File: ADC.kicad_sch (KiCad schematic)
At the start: 18 parts

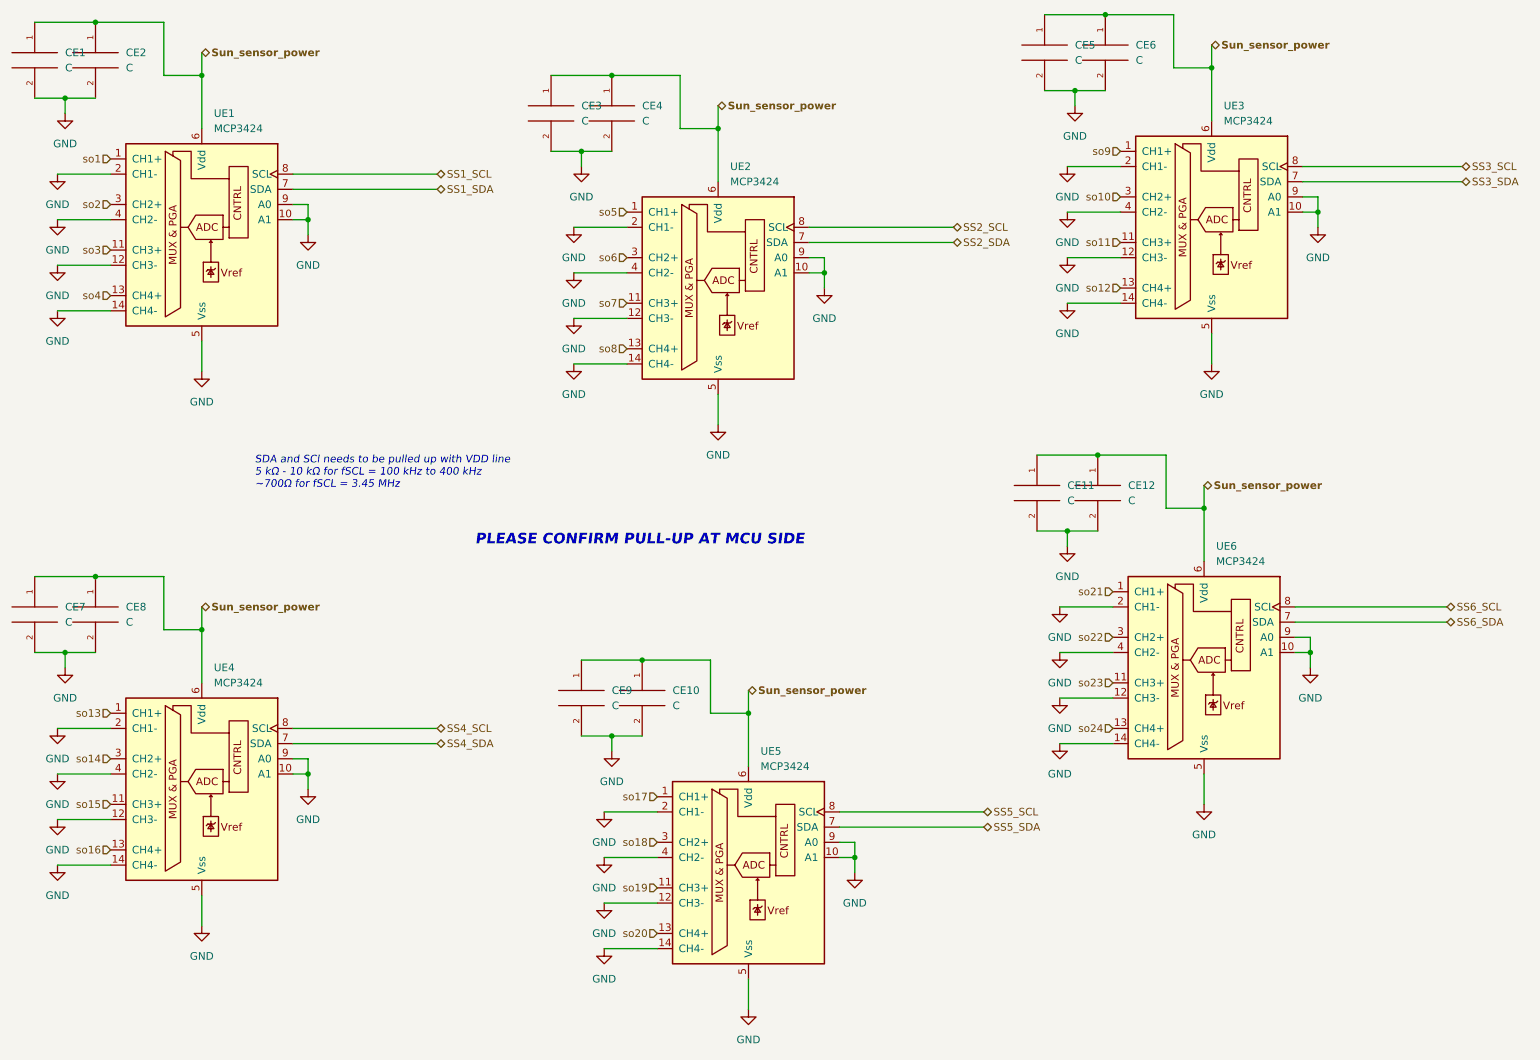
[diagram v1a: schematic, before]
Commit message: ADC Decaps added
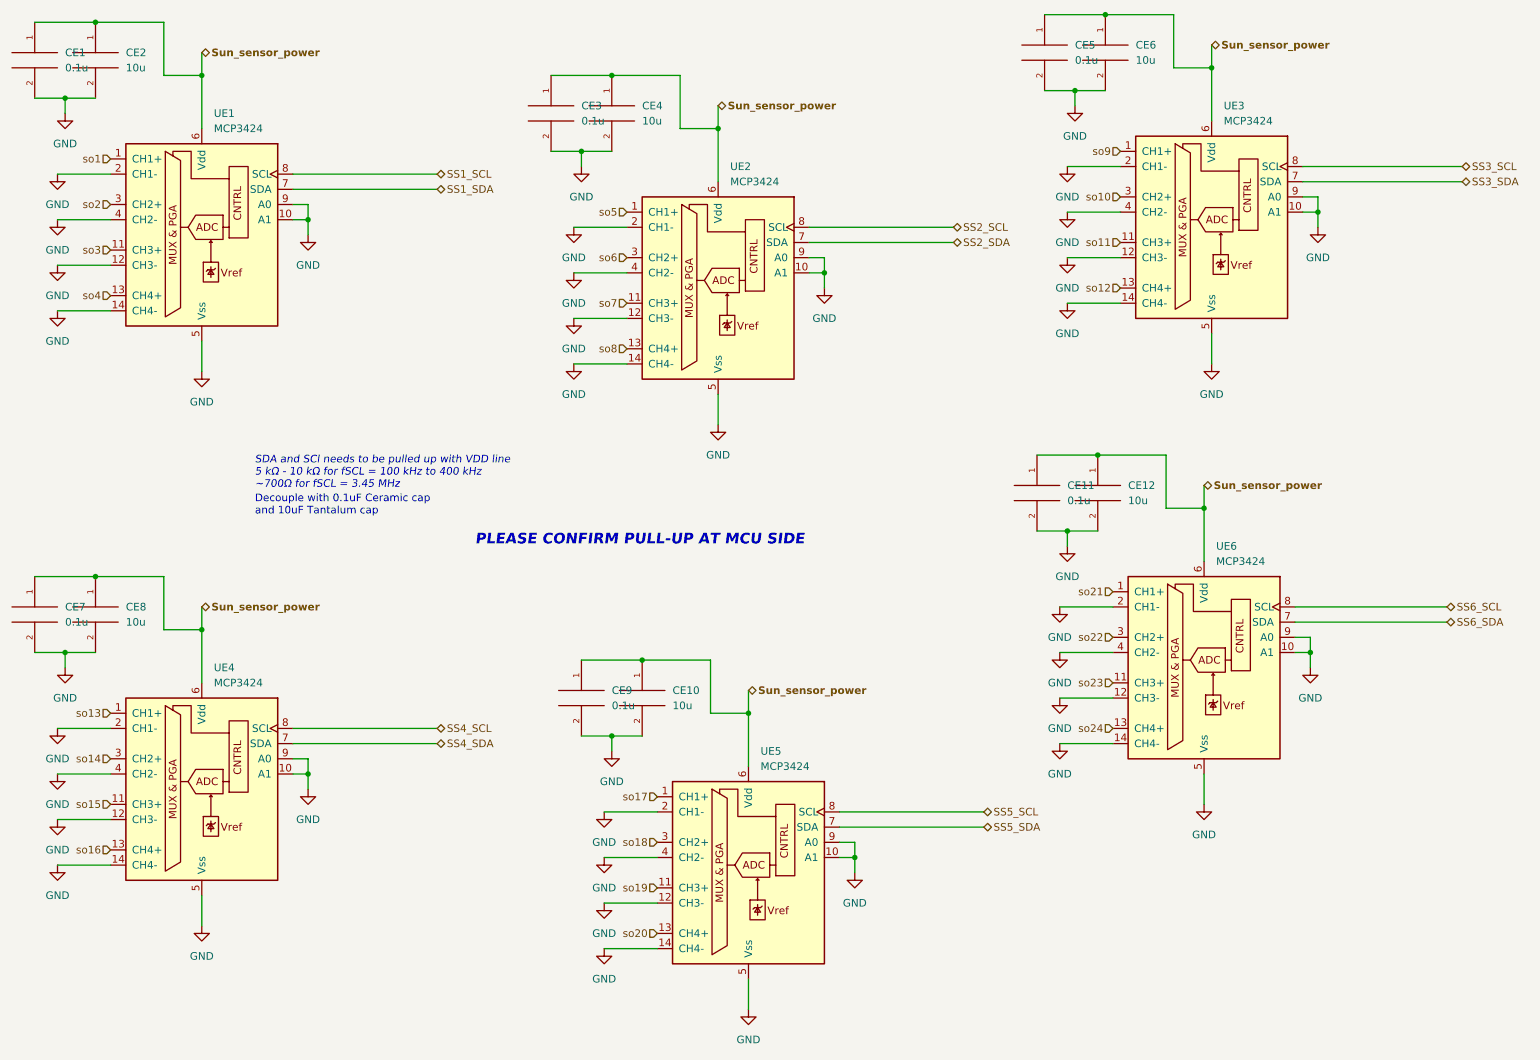
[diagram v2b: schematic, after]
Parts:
- CE1, CE11, CE3, CE5, CE7, CE9: value C -> 0.1u
- CE10, CE12, CE2, CE4, CE6, CE8: value C -> 10u
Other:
- note added: "Decouple with 0.1uF Ceramic cap and 10uF Tantalum cap"
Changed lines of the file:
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@@
     (effects (font (size 1.778 1.778) (thickness 0.3556) bold italic) (justify left bottom))
+  )
+  (text "Decouple with 0.1uF Ceramic cap \nand 10uF Tantalum cap \n"
+    (at 59.69 107.95 0)
+    (effects (font (size 1.27 1.27)) (justify left bottom))
   )
   (text "SDA and SCl needs to be pulled up with VDD line\n5 kΩ - 10 kΩ for fSCL = 100 kHz to 400 kHz\n~700Ω for fSCL = 3.45 MHz\n"
@@
       (effects (font (size 1.27 1.27)) (justify left))
     )
-    (property "Value" "C" (id 1) (at 129.54 139.6999 0)
+    (property "Value" "10u" (id 1) (at 129.54 139.6999 0)
       (effects (font (size 1.27 1.27)) (justify left))
     )
@@
       (effects (font (size 1.27 1.27)) (justify left))
     )
-    (property "Value" "C" (id 1) (at 114.3 41.9099 0)
+    (property "Value" "0.1u" (id 1) (at 114.3 41.9099 0)
       (effects (font (size 1.27 1.27)) (justify left))
     )
@@
       (effects (font (size 1.27 1.27)) (justify left))
     )
-    (property "Value" "C" (id 1) (at 119.38 139.6999 0)
+    (property "Value" "0.1u" (id 1) (at 119.38 139.6999 0)
       (effects (font (size 1.27 1.27)) (justify left))
     )
@@
       (effects (font (size 1.27 1.27)) (justify left))
     )
-    (property "Value" "C" (id 1) (at 38.1 33.0199 0)
+    (property "Value" "10u" (id 1) (at 38.1 33.0199 0)
       (effects (font (size 1.27 1.27)) (justify left))
     )
@@
       (effects (font (size 1.27 1.27)) (justify left))
     )
-    (property "Value" "C" (id 1) (at 196.85 31.7499 0)
+    (property "Value" "0.1u" (id 1) (at 196.85 31.7499 0)
       (effects (font (size 1.27 1.27)) (justify left))
     )
@@
       (effects (font (size 1.27 1.27)) (justify left))
     )
-    (property "Value" "C" (id 1) (at 195.58 105.4099 0)
+    (property "Value" "0.1u" (id 1) (at 195.58 105.4099 0)
       (effects (font (size 1.27 1.27)) (justify left))
     )
@@
       (effects (font (size 1.27 1.27)) (justify left))
     )
-    (property "Value" "C" (id 1) (at 27.94 125.7299 0)
+    (property "Value" "0.1u" (id 1) (at 27.94 125.7299 0)
       (effects (font (size 1.27 1.27)) (justify left))
     )
@@
       (effects (font (size 1.27 1.27)) (justify left))
     )
-    (property "Value" "C" (id 1) (at 207.01 31.7499 0)
+    (property "Value" "10u" (id 1) (at 207.01 31.7499 0)
       (effects (font (size 1.27 1.27)) (justify left))
     )
@@
       (effects (font (size 1.27 1.27)) (justify left))
     )
-    (property "Value" "C" (id 1) (at 38.1 125.7299 0)
+    (property "Value" "10u" (id 1) (at 38.1 125.7299 0)
       (effects (font (size 1.27 1.27)) (justify left))
     )
@@
       (effects (font (size 1.27 1.27)) (justify left))
     )
-    (property "Value" "C" (id 1) (at 124.46 41.9099 0)
+    (property "Value" "10u" (id 1) (at 124.46 41.9099 0)
       (effects (font (size 1.27 1.27)) (justify left))
     )
@@
       (effects (font (size 1.27 1.27)) (justify left))
     )
-    (property "Value" "C" (id 1) (at 205.74 105.4099 0)
+    (property "Value" "10u" (id 1) (at 205.74 105.4099 0)
       (effects (font (size 1.27 1.27)) (justify left))
     )
@@
       (effects (font (size 1.27 1.27)) (justify left))
     )
-    (property "Value" "C" (id 1) (at 27.94 33.0199 0)
-      (effects (font (size 1.27 1.27)) (justify left))
-    )
+    (property "Value" "0.1u" (id 1) (at 27.94 33.0199 0)
+      (effects (font (size 1.27 1.27)) (justify left))
+    )

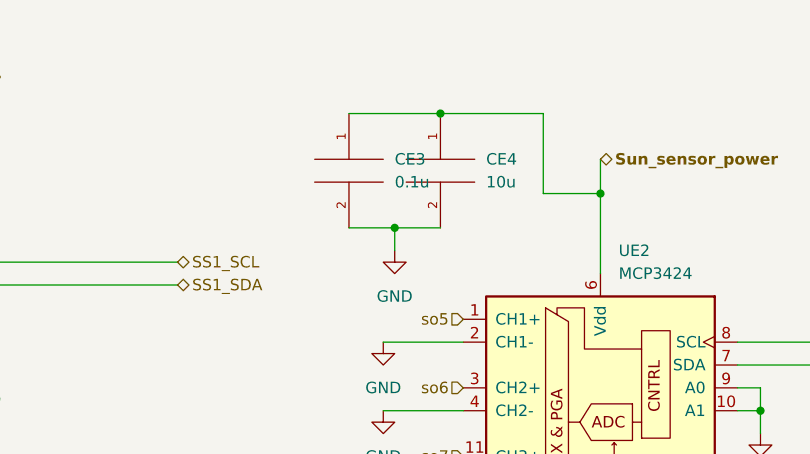
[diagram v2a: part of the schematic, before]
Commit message: Reset switch added
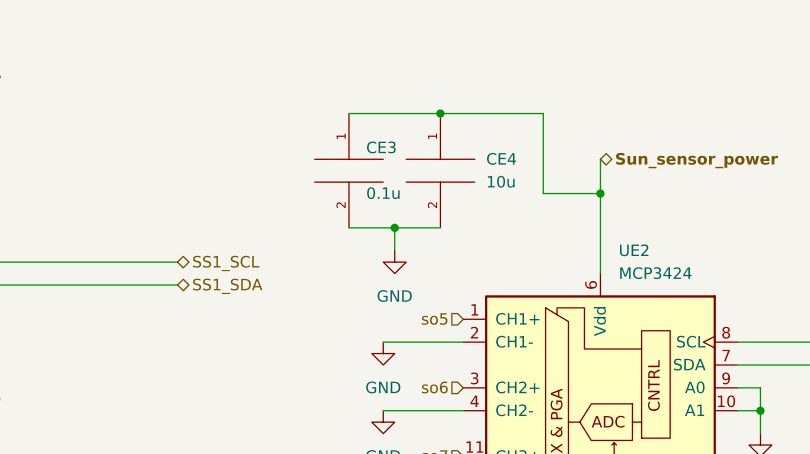
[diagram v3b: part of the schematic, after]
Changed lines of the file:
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@@
   )
   (symbol (lib_id "pspice:C") (at 109.22 40.64 0) (unit 1)
-    (in_bom yes) (on_board yes) (fields_autoplaced)
-    (property "Reference" "CE3" (id 0) (at 114.3 39.3699 0)
+    (in_bom yes) (on_board yes)
+    (property "Reference" "CE3" (id 0) (at 111.125 38.1 0)
       (effects (font (size 1.27 1.27)) (justify left))
     )
-    (property "Value" "0.1u" (id 1) (at 114.3 41.9099 0)
+    (property "Value" "0.1u" (id 1) (at 111.125 43.18 0)
       (effects (font (size 1.27 1.27)) (justify left))
     )

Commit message: MCU interfaces are done! Check the Changes and Complete ERC modifications
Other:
- company: (none) -> Parikshit Student Satellite Team
- title: (none) -> AOCS BOARD
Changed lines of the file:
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@@
 (kicad_sch (version 20211123) (generator eeschema)
   (paper "A4")
+  (title_block
+    (title "AOCS BOARD")
+    (company "Parikshit Student Satellite Team")
+  )
   (junction (at 201.93 24.13) (diameter 0) (color 0 0 0 0)
   )
@@
   )
   (wire (pts (xy 137.16 43.18) (xy 130.81 43.18))
+    (stroke (width 0) (type default) (color 0 0 0 0))
+  )
+  (wire (pts (xy 73.025 191.135) (xy 73.025 189.865))
     (stroke (width 0) (type default) (color 0 0 0 0))
   )
@@
     (pin "1")
   )
+  (symbol (lib_id "power:PWR_FLAG") (at 73.025 189.865 0) (unit 1)
+    (in_bom yes) (on_board yes) (fields_autoplaced)
+    (property "Reference" "#FLG0112" (id 0) (at 73.025 187.96 0)
+      (effects (font (size 1.27 1.27)) hide)
+    )
+    (property "Value" "PWR_FLAG" (id 1) (at 73.025 184.15 0))
+    (property "Footprint" "" (id 2) (at 73.025 189.865 0)
+      (effects (font (size 1.27 1.27)) hide)
+    )
+    (property "Datasheet" "~" (id 3) (at 73.025 189.865 0)
+      (effects (font (size 1.27 1.27)) hide)
+    )
+    (pin "1")
+  )
   (symbol (lib_id "power:GND") (at 119.38 147.32 0) (unit 1)
     (in_bom yes) (on_board yes) (fields_autoplaced)
@@
       (effects (font (size 1.27 1.27)) hide)
     )
+    (pin "1")
+  )
+  (symbol (lib_id "power:GND") (at 73.025 191.135 0) (unit 1)
+    (in_bom yes) (on_board yes) (fields_autoplaced)
+    (property "Reference" "#PWR0276" (id 0) (at 73.025 197.485 0)
+      (effects (font (size 1.27 1.27)) hide)
+    )
+    (property "Value" "GND" (id 1) (at 73.025 195.58 0))
+    (property "Footprint" "" (id 2) (at 73.025 191.135 0)
+      (effects (font (size 1.27 1.27)) hide)
+    )
+    (property "Datasheet" "" (id 3) (at 73.025 191.135 0)
+      (effects (font (size 1.27 1.27)) hide)
+    )

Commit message: Updated the changes
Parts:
- renumbered CE5 to CE1, CE8 to CE10, CE9 to CE11, CE10 to CE12, CE6 to CE2, CE1 to CE3, CE2 to CE4, CE3 to CE5, CE4 to CE6, CE11 to CE7, CE12 to CE8, CE7 to CE9, UE3 to UE1, UE1 to UE2, UE2 to UE3, UE6 to UE4, UE4 to UE5, UE5 to UE6

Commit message: Page settings changed. Added some testpoints. Some comments are made.
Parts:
- renumbered CE3 to CE1, CE1 to CE10, CE8 to CE11, CE2 to CE12, CE9 to CE2, CE4 to CE3, CE10 to CE4, CE11 to CE6, CE6 to CE7, CE12 to CE8, CE7 to CE9, UE2 to UE1, UE5 to UE2, UE6 to UE4, UE4 to UE5, UE1 to UE6

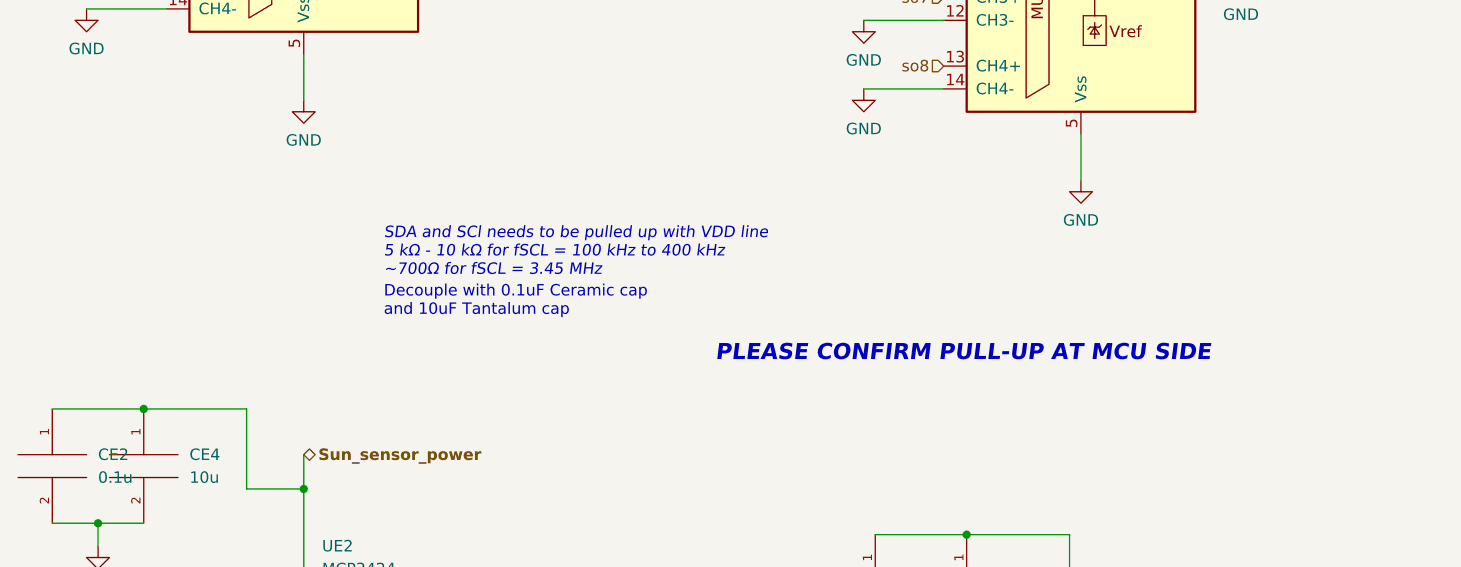
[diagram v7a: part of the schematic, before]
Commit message: I2C lines are pulled up
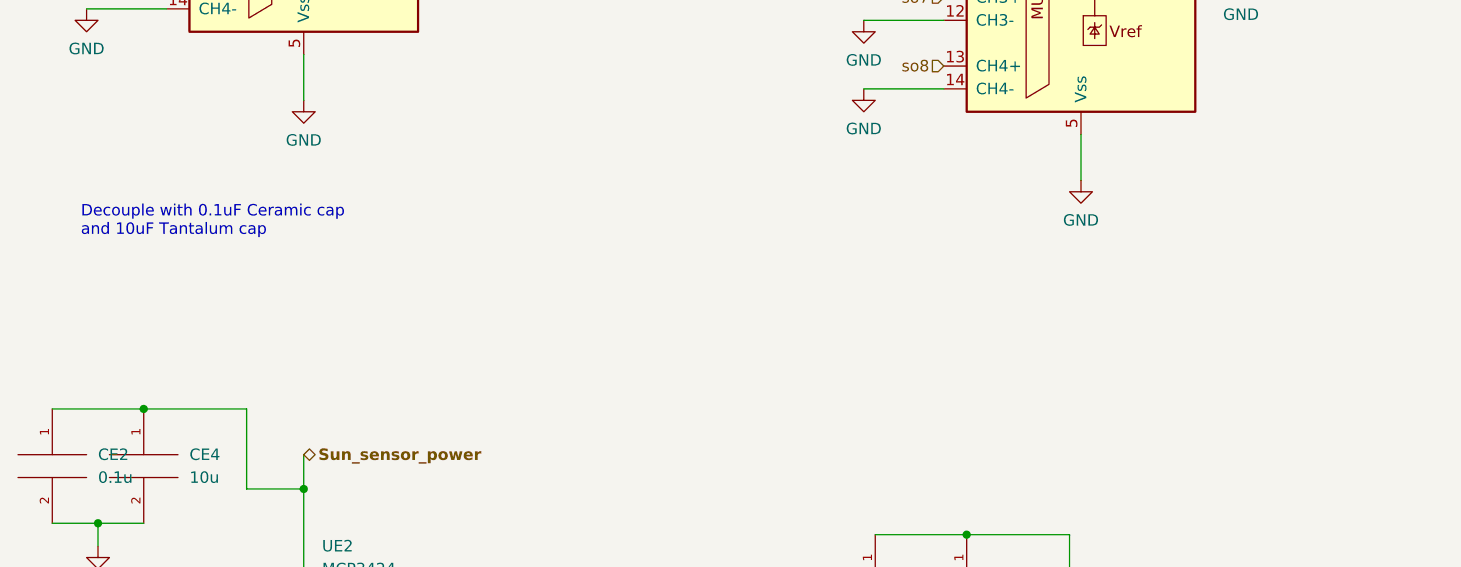
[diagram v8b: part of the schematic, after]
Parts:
- CE1, CE10, CE2, CE5, CE6, CE9: footprint (none) -> Capacitor_SMD:C_0603_1608Metric
- CE11: footprint (none) -> Capacitor_Tantalum_SMD:CP_EIA-7132-20_AVX-U
- CE12: footprint (none) -> Capacitor_Tantalum_SMD:CP_EIA-7132-20_AVX-U_Pad2.72x3.50mm_HandSolder
- CE3, CE4, CE7, CE8: footprint (none) -> Capacitor_Tantalum_SMD:CP_EIA-6032-28_Kemet-C_Pad2.25x2.35mm_HandSolder
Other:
- note removed: "PLEASE CONFIRM PULL-UP AT MCU SIDE"
- note removed: "SDA and SCl needs to be pulled up with VDD line 5 kΩ - 10 kΩ for fSCL = 100 kHz to 400 kHz ~700Ω for fSCL = 3.45 MHz"
